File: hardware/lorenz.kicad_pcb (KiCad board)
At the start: 2 copper layers, 100 x 100 mm, 86 parts, among them J1 USB-C, J2 BNC, J3 BNC, J4 BNC, SW1 SW_DIP_x06, U1 LF412, U2 LF412, U3 MPY634, U4 MPY634, U5 A0515S-2WR2, U6 78L12, U7 79L12

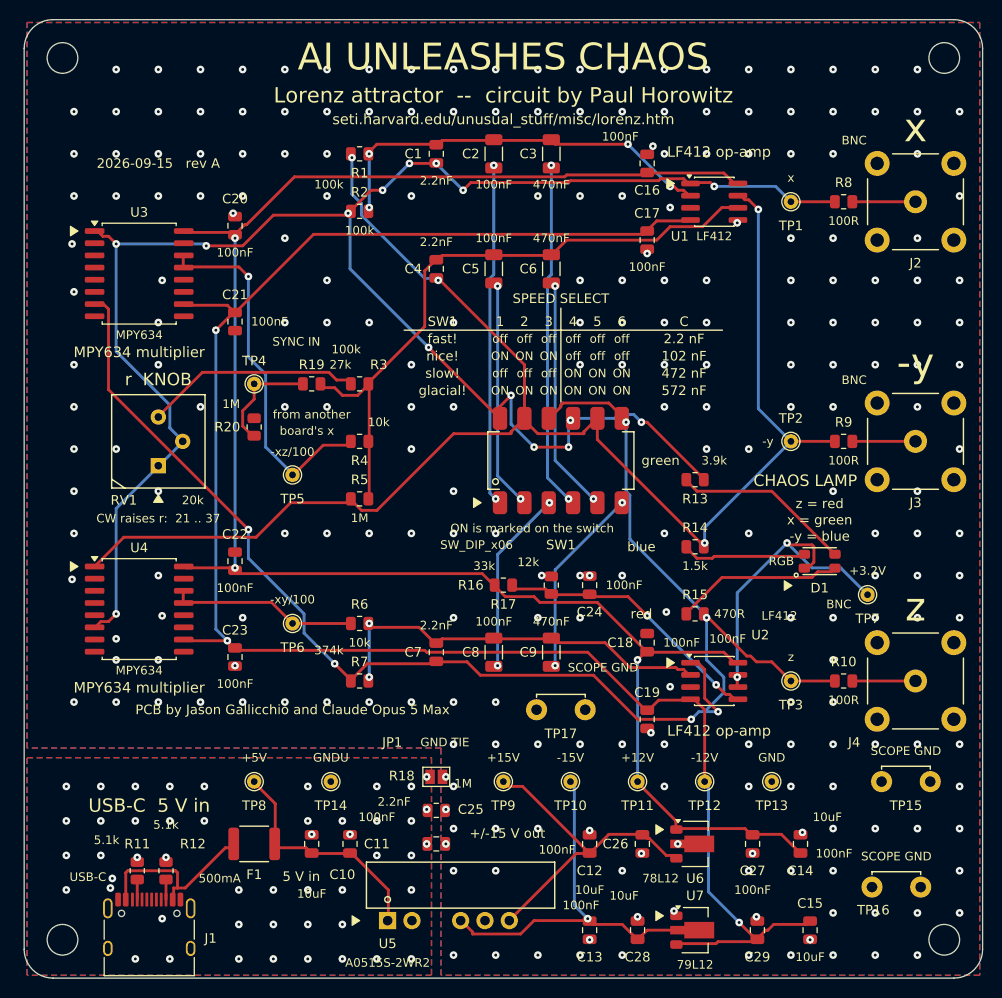
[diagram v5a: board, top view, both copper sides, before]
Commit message: Give SYNC IN X its own BNC, a weight knob, and a drawing that adds up
SYNC IN is now SYNC IN X everywhere: a fourth BNC on the left edge, in
line with the x output on the right, because another board's x output is
what goes in it.  RV2 sets how much of it gets in.

RV2 is a divider across the incoming signal rather than a rheostat in
series with R19, which makes the weight linear in the knob --
g = 1M/100k x (fraction turned) = 0 to 10 -- instead of hyperbolic.  A
rheostat would have crammed the locking threshold, about g = 7, into the
first tenth of the rotation; as a divider it lands at 70 %, so the bottom
seven tenths is "never quite" and the top three tenths locks in a couple
of seconds at slow!.  At the counter-clockwise stop the wiper sits on
ground and the branch contributes nothing, which is the same thing as
unplugging the cable.

The drawing now says what the circuit means.  Row 2's branches run -y,
x z, x down the sheet, and the x branch and the sync branch join on their
own rail before that rail reaches the summing junction: a perturbation on
the x term, not a fourth term.  On the board R19 is the next resistor
down the column from R3, with "SYNC IN X adds here" beside it, and the
whole chain -- jack, knob, resistor -- runs left to right into the
column.  The multipliers moved 9 mm right to make room, and the back's
equations shrank to clear the drilled parts down that edge.

Also: the pin-1 triangles are back to the four parts whose own footprints
have no legible mark (D1, SW1, RV1, RV2) rather than every rotatable
part; poles 1-3 now carry the 470 nF and 4-6 the 100 nF so the six
sliders read left to right as a binary number; "glacial!" is "slower!";
the credit line and the circuit URL swapped places, with the date and
revision under the credit at 0.9 mm; and the owl caption says 'scope.

Co-Authored-By: Claude Opus 5 <noreply@anthropic.com>
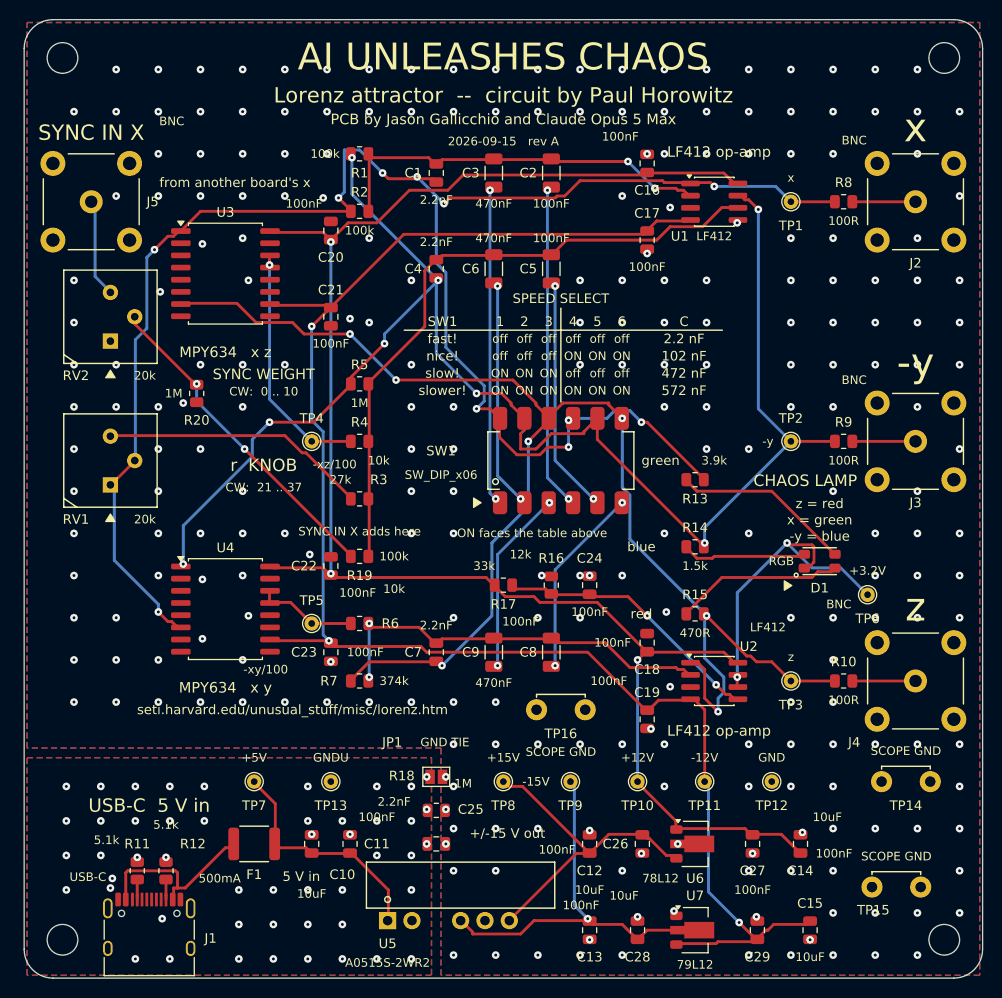
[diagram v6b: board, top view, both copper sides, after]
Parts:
- removed TP17: SCOPE GND, lorenz:TestPoint_ScopeGnd_Loop_2x1.1mm
- added J5: BNC, lorenz:BNC_KYWE_RightAngle, F.Cu at (7.00, 19.0)
- added RV2: 20k, lorenz:Potentiometer_Bourns_3386P_Vertical, F.Cu at (9.00, 33.5)
- TP10: value -15V -> +12V
- TP11: value +12V -> -12V
- TP12: value -12V -> GND
- TP13: value GND -> GNDU
- TP14: value GNDU -> SCOPE GND; footprint TestPoint:TestPoint_THTPad_D1.5mm_Drill0.7mm -> lorenz:TestPoint_ScopeGnd_Loop_2x1.1mm
- TP4: value SYNC IN -> -xz/100
- TP5: value -xz/100 -> -xy/100
- TP6: value -xy/100 -> +3.2V
- TP7: value +3.2V -> +5V
- TP8: value +5V -> +15V
- TP9: value +15V -> -15V
- moved TP7 66.9 mm to (24.0, 79.5)
- moved TP6 60.1 mm to (88.0, 60.0)
- moved TP14 60.0 mm to (92.0, 79.5)
- moved TP13 46.0 mm to (32.0, 79.5)
- moved TP16 39.6 mm to (56.0, 72.0)
- moved TP8 26.0 mm to (50.0, 79.5)
- moved R19 18.7 mm to (35.0, 56.0)
- moved TP5 15.6 mm to (30.0, 63.0)
- moved R3 12.0 mm to (35.0, 50.0)
- moved R5 12.0 mm to (35.0, 38.0)
- moved TP15 11.0 mm to (91.0, 90.5)
- moved C20 10.0 mm to (32.0, 22.0)
- moved C21 10.0 mm to (32.0, 31.0)
- moved C22 10.0 mm to (32.0, 57.0)
- moved C23 10.0 mm to (32.0, 66.0)
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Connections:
- R20 pad 1: Net-(R19-Pad1) -> GND
- R20 pad 2: GND -> Net-(R19-Pad1)
- SW1 pad 1: Net-(C2-Pad1) -> Net-(C3-Pad1)
- SW1 pad 2: Net-(C5-Pad1) -> Net-(C6-Pad1)
- SW1 pad 3: Net-(C8-Pad1) -> Net-(C9-Pad1)
- SW1 pad 4: Net-(C3-Pad1) -> Net-(C2-Pad1)
- SW1 pad 5: Net-(C6-Pad1) -> Net-(C5-Pad1)
- SW1 pad 6: Net-(C9-Pad1) -> Net-(C8-Pad1)
- TP10 pad 1: -15V -> +12V
- TP11 pad 1: +12V -> -12V
- TP12 pad 1: -12V -> GND
- TP13 pad 1: GND -> GNDU
- TP14 pad 1: GNDU -> GND
- TP4 pad 1: Net-(R19-Pad1) -> /xz
- TP5 pad 1: /xz -> /xy
- TP6 pad 1: /xy -> Net-(D1-A)
- TP7 pad 1: Net-(D1-A) -> +5V
- TP8 pad 1: +5V -> +15V
- TP9 pad 1: +15V -> -15V
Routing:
- net Net-(R19-Pad1): track 11.6 -> 34.5 mm, vias 0 -> 2
- net +12V: track 192.5 -> 174.9 mm
- net -12V: track 192.1 -> 174.7 mm
- net /xz: track 38.6 -> 25.6 mm
- net Net-(J5-In): track 0.00 -> 10.3 mm
- net /z: track 161.7 -> 152.4 mm, vias 6 -> 7
- net /xy: track 19.7 -> 10.7 mm
- net Net-(R3-Pad1): track 22.6 -> 27.9 mm
- net /-y: track 163.7 -> 158.9 mm, vias 4 -> 8
- net Net-(C3-Pad1): track 36.8 -> 33.6 mm
- net /x: track 192.8 -> 190.5 mm, vias 15 -> 11
- net Net-(C2-Pad1): track 36.1 -> 34.2 mm
- net /SJ_X: track 42.8 -> 41.8 mm, vias 4 -> 2
- net Net-(C6-Pad1): track 24.9 -> 24.3 mm
- net Net-(C5-Pad1): track 24.3 -> 24.9 mm
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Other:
- board text added: "CW: 0 .. 10"
- board text added: "CW: 21 .. 37"
- board text added: "MPY634 x y"
- board text added: "MPY634 x z"
- board text added: "ON faces the table above"
- board text added: "SYNC IN X"
- board text added: "SYNC IN X adds here"
- board text added: "SYNC WEIGHT"
- board text added: "from another board's x"
- board text added: "put x and z on 'scope X-Y to see this"
- board text added: "r = 21 to 37 on the knob"
- board text added: "s = 10 b = 8/3"
- board text added: "slower!"
- board text removed: "CW raises r: 21 .. 37"
- board text removed: "MPY634 multiplier"
- board text removed: "ON is marked on the switch"
- board text removed: "board's x"
- board text removed: "from another"
- board text removed: "glacial!"
- board text removed: "put x and z on X-Y to see this"
- board text removed: "s = 10 r = 21 to 37 b = 8/3"

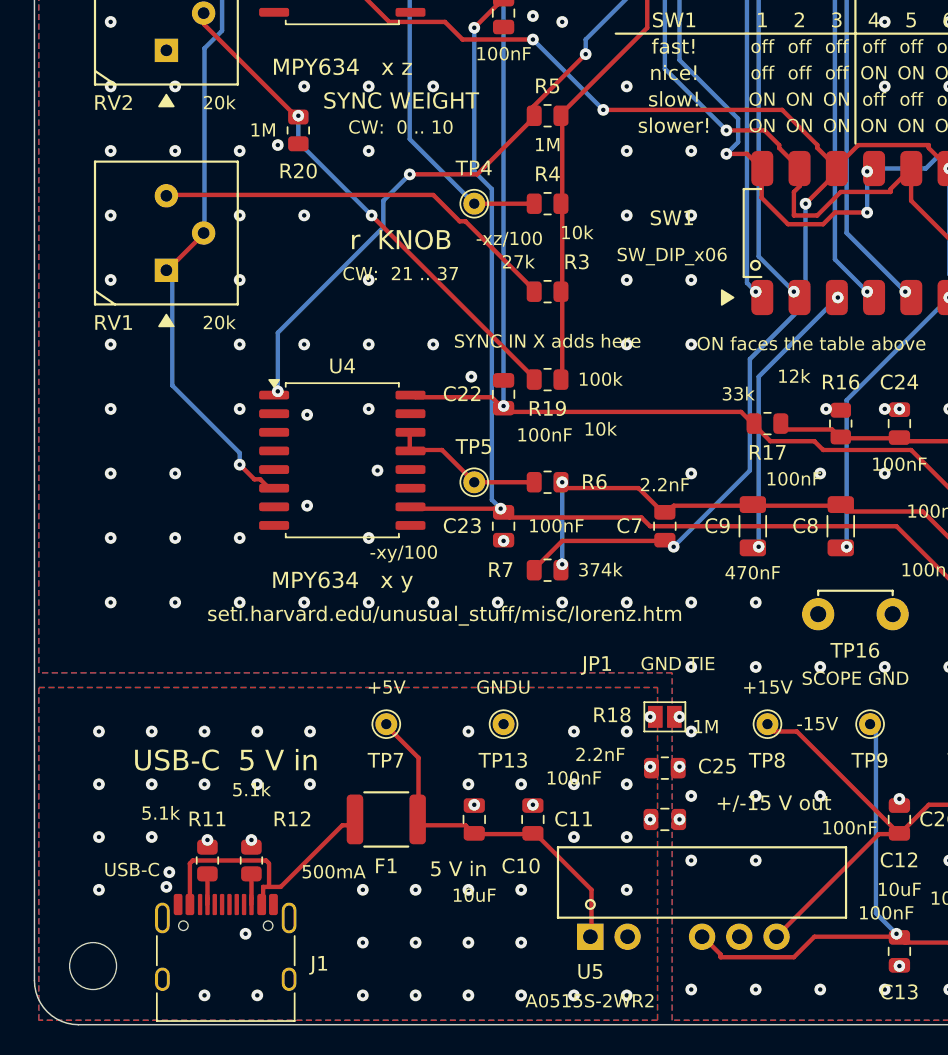
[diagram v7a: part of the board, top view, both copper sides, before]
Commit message: Put the pick-and-place point on the part, and turn six of them for JLC
RV1, RV2 and U5 were drawn off their own pads in JLCPCB's preview, and no
rotation fixed it because it was not a rotation.  A CPL says where the
*middle* of a part goes; those three footprints are mine, and I had put
the anchor on pin 1 -- 2.54 mm out for the trimmers, 7.6 mm across and
2.6 mm down for the DC/DC module.  Both footprints now anchor on the
centre of the body, and their placements moved by the same amount the
other way, so every copper, mask, paste, drill and outline file is
byte-identical; only the CPL and two silkscreen designators change.

JLCPCB places from its own model of a part, and for six of ours that
model is turned differently from KiCad's footprint, so the build now also
writes out/<board>/<board>-cpl_jlc_corrected.csv: the same placements
with the measured per-part angles applied, keyed by LCSC number because
the angle belongs to JLC's drawing of that part rather than to its
package.  check_outputs proves the two files differ in nothing but those
angles.  Four parts whose angle has never been readable -- D1, RV1, RV2,
U5 -- are deliberately left uncorrected and called out for checking.

docs/MANUFACTURING.md gains an "Uploading to JLCPCB" section: which file
goes where, the rotation table, the unverified four, and what an
unknown-part checkerboard actually means -- harmless on R7, which is a
resistor, and worth a note on the order or a hand-soldered lamp for D1,
which is polarised.

Co-Authored-By: Claude Opus 5 <noreply@anthropic.com>
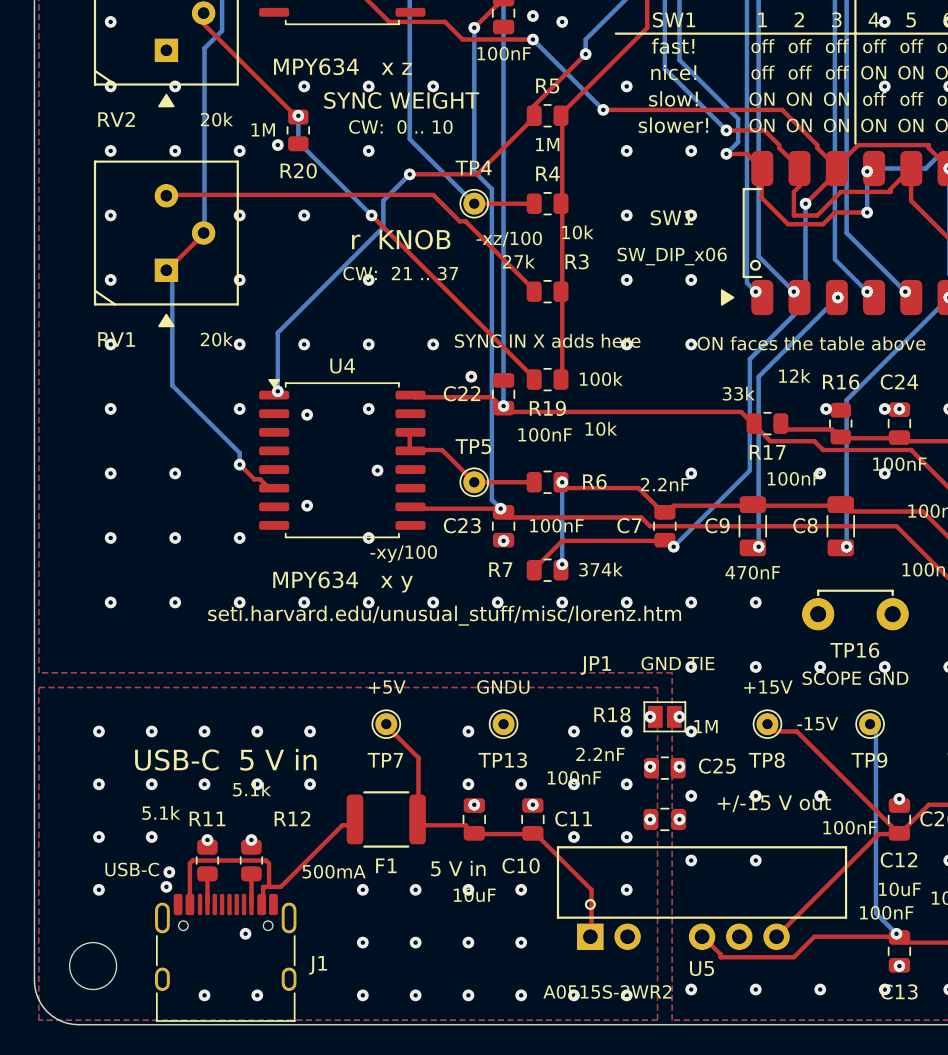
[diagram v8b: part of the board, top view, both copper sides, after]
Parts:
- moved U5 8.05 mm to (45.5, 91.4)
- moved RV1 2.54 mm to (9.00, 46.0)
- moved RV2 2.54 mm to (9.00, 31.0)
